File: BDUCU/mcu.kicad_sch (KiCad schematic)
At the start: 15 parts, among them SW1 SW_Push, U8 ATmega328-A, Y1 20MHz

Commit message: BDUCU did stuffs
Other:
- added sheet CAN1 (can_controller.kicad_sch)
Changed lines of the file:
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@@
     )
   )
-  (global_label "CAN0_CS" (shape output) (at 209.55 46.736 180) (fields_autoplaced)
-    (effects (font (size 1.27 1.27)) (justify right))
-    (property "Intersheetrefs" "${INTERSHEET_REFS}" (at 198.2191 46.736 0)
+  (global_label "CAN0_CS" (shape output) (at 209.55 46.355 180) (fields_autoplaced)
+    (effects (font (size 1.27 1.27)) (justify right))
+    (property "Intersheetrefs" "${INTERSHEET_REFS}" (at 198.2191 46.355 0)
       (effects (font (size 1.27 1.27)) (justify right) hide)
     )
@@
     )
   )
+  (global_label "CAN0_H" (shape input) (at 242.57 43.815 0) (fields_autoplaced)
+    (effects (font (size 1.27 1.27)) (justify left))
+    (property "Intersheetrefs" "${INTERSHEET_REFS}" (at 252.7519 43.815 0)
+      (effects (font (size 1.27 1.27)) (justify left) hide)
+    )
+  )
+  (global_label "SCK" (shape output) (at 209.55 66.675 180) (fields_autoplaced)
+    (effects (font (size 1.27 1.27)) (justify right))
+    (property "Intersheetrefs" "${INTERSHEET_REFS}" (at 202.8153 66.675 0)
+      (effects (font (size 1.27 1.27)) (justify right) hide)
+    )
+  )
   (global_label "TS_ACT_5" (shape input) (at 71.374 104.648 0) (fields_autoplaced)
     (effects (font (size 1.27 1.27)) (justify left))
@@
     )
   )
+  (global_label "CAN1_CS" (shape output) (at 209.55 63.5 180) (fields_autoplaced)
+    (effects (font (size 1.27 1.27)) (justify right))
+    (property "Intersheetrefs" "${INTERSHEET_REFS}" (at 198.2191 63.5 0)
+      (effects (font (size 1.27 1.27)) (justify right) hide)
+    )
+  )
   (global_label "RST" (shape input) (at 114.935 117.475 180) (fields_autoplaced)
     (effects (font (size 1.27 1.27)) (justify right))
@@
     )
   )
+  (global_label "MOSI" (shape input) (at 209.55 60.96 180) (fields_autoplaced)
+    (effects (font (size 1.27 1.27)) (justify right))
+    (property "Intersheetrefs" "${INTERSHEET_REFS}" (at 202.048 60.96 0)
+      (effects (font (size 1.27 1.27)) (justify right) hide)
+    )
+  )
   (global_label "AIR+_5" (shape output) (at 71.374 94.488 0) (fields_autoplaced)
     (effects (font (size 1.27 1.27)) (justify left))
@@
     )
   )
+  (global_label "MISO" (shape output) (at 209.55 58.42 180) (fields_autoplaced)
+    (effects (font (size 1.27 1.27)) (justify right))
+    (property "Intersheetrefs" "${INTERSHEET_REFS}" (at 201.9686 58.42 0)
+      (effects (font (size 1.27 1.27)) (justify right) hide)
+    )
+  )
   (global_label "HALL_HI" (shape input) (at 71.374 79.248 0) (fields_autoplaced)
     (effects (font (size 1.27 1.27)) (justify left))
@@
     )
   )
+  (global_label "CAN1_H" (shape input) (at 242.57 60.325 0) (fields_autoplaced)
+    (effects (font (size 1.27 1.27)) (justify left))
+    (property "Intersheetrefs" "${INTERSHEET_REFS}" (at 252.7519 60.325 0)
+      (effects (font (size 1.27 1.27)) (justify left) hide)
+    )
+  )
   (global_label "MOSI" (shape input) (at 71.374 56.388 0) (fields_autoplaced)
     (effects (font (size 1.27 1.27)) (justify left))
@@
     )
   )
-  (global_label "MOSI" (shape input) (at 209.55 44.196 180) (fields_autoplaced)
-    (effects (font (size 1.27 1.27)) (justify right))
-    (property "Intersheetrefs" "${INTERSHEET_REFS}" (at 202.048 44.196 0)
+  (global_label "MOSI" (shape input) (at 209.55 43.815 180) (fields_autoplaced)
+    (effects (font (size 1.27 1.27)) (justify right))
+    (property "Intersheetrefs" "${INTERSHEET_REFS}" (at 202.048 43.815 0)
       (effects (font (size 1.27 1.27)) (justify right) hide)
     )
@@
     )
   )
+  (global_label "CAN0_L" (shape input) (at 242.57 46.355 0) (fields_autoplaced)
+    (effects (font (size 1.27 1.27)) (justify left))
+    (property "Intersheetrefs" "${INTERSHEET_REFS}" (at 252.4495 46.355 0)
+      (effects (font (size 1.27 1.27)) (justify left) hide)
+    )
+  )
   (global_label "CAN0_CS" (shape output) (at 71.374 53.848 0) (fields_autoplaced)
     (effects (font (size 1.27 1.27)) (justify left))
@@
     )
   )
-  (global_label "SCK" (shape output) (at 209.55 49.53 180) (fields_autoplaced)
-    (effects (font (size 1.27 1.27)) (justify right))
-    (property "Intersheetrefs" "${INTERSHEET_REFS}" (at 202.8153 49.53 0)
-      (effects (font (size 1.27 1.27)) (justify right) hide)
-    )
-  )
-  (global_label "MISO" (shape output) (at 209.55 41.656 180) (fields_autoplaced)
-    (effects (font (size 1.27 1.27)) (justify right))
-    (property "Intersheetrefs" "${INTERSHEET_REFS}" (at 201.9686 41.656 0)
+  (global_label "SCK" (shape output) (at 209.55 48.895 180) (fields_autoplaced)
+    (effects (font (size 1.27 1.27)) (justify right))
+    (property "Intersheetrefs" "${INTERSHEET_REFS}" (at 202.8153 48.895 0)
+      (effects (font (size 1.27 1.27)) (justify right) hide)
+    )
+  )
+  (global_label "CAN1_L" (shape input) (at 242.57 62.865 0) (fields_autoplaced)
+    (effects (font (size 1.27 1.27)) (justify left))
+    (property "Intersheetrefs" "${INTERSHEET_REFS}" (at 252.4495 62.865 0)
+      (effects (font (size 1.27 1.27)) (justify left) hide)
+    )
+  )
+  (global_label "MISO" (shape output) (at 209.55 41.275 180) (fields_autoplaced)
+    (effects (font (size 1.27 1.27)) (justify right))
+    (property "Intersheetrefs" "${INTERSHEET_REFS}" (at 201.9686 41.275 0)
       (effects (font (size 1.27 1.27)) (justify right) hide)
     )
@@
     )
   )
-  (sheet (at 209.55 39.624) (size 33.274 11.43) (fields_autoplaced)
+  (sheet (at 209.55 39.37) (size 33.02 11.43) (fields_autoplaced)
     (stroke (width 0.1524) (type solid))
     (fill (color 0 0 0 0.0000))
-    (property "Sheetname" "CAN0" (at 209.55 38.9124 0)
+    (property "Sheetname" "CAN0" (at 209.55 38.6584 0)
       (effects (font (size 1.27 1.27)) (justify left bottom))
     )
-    (property "Sheetfile" "can_controller.kicad_sch" (at 209.55 51.6386 0)
+    (property "Sheetfile" "can_controller.kicad_sch" (at 209.55 51.3846 0)
       (effects (font (size 1.27 1.27)) (justify left top))
     )
-    (pin "MISO" input (at 209.55 41.656 180)
+    (pin "MISO" input (at 209.55 41.275 180)
       (effects (font (size 1.27 1.27)) (justify left))
     )
-    (pin "MOSI" input (at 209.55 44.196 180)
+    (pin "MOSI" input (at 209.55 43.815 180)
       (effects (font (size 1.27 1.27)) (justify left))
     )
-    (pin "CS" input (at 209.55 46.736 180)
+    (pin "CS" input (at 209.55 46.355 180)
       (effects (font (size 1.27 1.27)) (justify left))
     )
-    (pin "SCK" input (at 209.55 49.53 180)
+    (pin "SCK" input (at 209.55 48.895 180)
       (effects (font (size 1.27 1.27)) (justify left))
     )
-    (pin "CAN_H" input (at 242.824 43.688 0)
-      (effects (font (size 1.27 1.27)) (justify right))
-    )
-    (pin "CAN_L" input (at 242.824 46.228 0)
+    (pin "CAN_H" input (at 242.57 43.815 0)
+      (effects (font (size 1.27 1.27)) (justify right))
+    )
+    (pin "CAN_L" input (at 242.57 46.355 0)
       (effects (font (size 1.27 1.27)) (justify right))
     )
@@
       )
     )
+  )
+  (sheet (at 209.55 56.515) (size 33.02 11.43) (fields_autoplaced)
+    (stroke (width 0.1524) (type solid))
+    (fill (color 0 0 0 0.0000))
+    (property "Sheetname" "CAN1" (at 209.55 55.8034 0)
+      (effects (font (size 1.27 1.27)) (justify left bottom))
+    )
+    (property "Sheetfile" "can_controller.kicad_sch" (at 209.55 68.5296 0)
+      (effects (font (size 1.27 1.27)) (justify left top))
+    )
+    (pin "MISO" input (at 209.55 58.42 180)
+      (effects (font (size 1.27 1.27)) (justify left))
+    )
+    (pin "MOSI" input (at 209.55 60.96 180)
+      (effects (font (size 1.27 1.27)) (justify left))
+    )
+    (pin "CS" input (at 209.55 63.5 180)
+      (effects (font (size 1.27 1.27)) (justify left))
+    )
+    (pin "SCK" input (at 209.55 66.675 180)
+      (effects (font (size 1.27 1.27)) (justify left))
+    )
+    (pin "CAN_H" input (at 242.57 60.325 0)
+      (effects (font (size 1.27 1.27)) (justify right))
+    )
+    (pin "CAN_L" input (at 242.57 62.865 0)
+      (effects (font (size 1.27 1.27)) (justify right))
+    )
+    (instances
+      (project "BDUCU"
+        (path "/9942a424-e19d-4ffb-8473-f960b5c811cf/8fc427df-2d97-44b9-b479-5014f2f05880" (page "12"))
+      )
+    )

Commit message: BDUCU COMMIT
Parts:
- AVR-ISP1: footprint Connector_PinHeader_2.54mm:PinHeader_2x03_P2.54mm_Vertical -> Connector_PinHeader_2.54mm:PinHeader_2x03_P2.54mm_Vertical_SMD
- Y1: value 20MHz -> 16MHz
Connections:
- net +5VA is gone; now on net +5V: C20.2, U8.20 (AREF)
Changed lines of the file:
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@@
 	)
 	(junction
-		(at 34.001 48.768)
+		(at 34.29 48.5525)
 		(diameter 0)
 		(color 0 0 0 0)
@@
 	(wire
 		(pts
-			(xy 34.001 48.768) (xy 40.894 48.768)
+			(xy 28.483 48.6795) (xy 33.563 48.6795)
+		)
+		(stroke
+			(width 0)
+			(type default)
+		)
+	)
+	(wire
+		(pts
+			(xy 34.29 48.5525) (xy 38.643 48.5525)
 		)
 		(stroke
@@
 	(wire
 		(pts
-			(xy 34.001 45.9355) (xy 34.001 48.768)
+			(xy 34.29 45.72) (xy 34.29 48.5525)
+		)
+		(stroke
+			(width 0)
+			(type default)
+		)
+	)
+	(wire
+		(pts
+			(xy 28.483 48.895) (xy 29.464 48.895)
 		)
 		(stroke
@@
 	(wire
 		(pts
+			(xy 28.483 48.6795) (xy 28.483 48.895)
+		)
+		(stroke
+			(width 0)
+			(type default)
+		)
+	)
+	(wire
+		(pts
 			(xy 111.76 86.995) (xy 111.76 95.25)
 		)
@@
 	(wire
 		(pts
-			(xy 33.274 48.895) (xy 33.274 48.768)
+			(xy 33.563 48.6795) (xy 33.563 48.5525)
 		)
 		(stroke
@@
 	(wire
 		(pts
+			(xy 38.643 48.768) (xy 40.894 48.768)
+		)
+		(stroke
+			(width 0)
+			(type default)
+		)
+	)
+	(wire
+		(pts
 			(xy 100.965 41.275) (xy 100.965 40.64)
 		)
@@
 	(wire
 		(pts
+			(xy 38.643 48.5525) (xy 38.643 48.768)
+		)
+		(stroke
+			(width 0)
+			(type default)
+		)
+	)
+	(wire
+		(pts
 			(xy 125.73 86.995) (xy 125.73 95.25)
 		)
@@
 	(wire
 		(pts
-			(xy 33.274 48.768) (xy 34.001 48.768)
-		)
-		(stroke
-			(width 0)
-			(type default)
-		)
-	)
-	(wire
-		(pts
-			(xy 29.464 48.895) (xy 33.274 48.895)
+			(xy 33.563 48.5525) (xy 34.29 48.5525)
 		)
 		(stroke
@@
 				(path "/9942a424-e19d-4ffb-8473-f960b5c811cf/8fc427df-2d97-44b9-b479-5014f2f05880"
 					(reference "D3")
+					(unit 1)
+				)
+			)
+		)
+	)
+	(symbol
+		(lib_id "power:+5V")
+		(at 34.29 45.72 0)
+		(unit 1)
+		(exclude_from_sim no)
+		(in_bom yes)
+		(on_board yes)
+		(dnp no)
+		(fields_autoplaced yes)
+		(property "Reference" "#PWR033"
+			(at 34.29 49.53 0)
+			(effects
+				(font
+					(size 1.27 1.27)
+				)
+				(hide yes)
+			)
+		)
+		(property "Value" "+5V"
+			(at 34.29 40.64 0)
+			(effects
+				(font
+					(size 1.27 1.27)
+				)
+			)
+		)
+		(property "Footprint" ""
+			(at 34.29 45.72 0)
+			(effects
+				(font
+					(size 1.27 1.27)
+				)
+				(hide yes)
+			)
+		)
+		(property "Datasheet" ""
+			(at 34.29 45.72 0)
+			(effects
+				(font
+					(size 1.27 1.27)
+				)
+				(hide yes)
+			)
+		)
+		(property "Description" ""
+			(at 34.29 45.72 0)
+			(effects
+				(font
+					(size 1.27 1.27)
+				)
+			)
+		)
+		(pin "1"
+		)
+		(instances
+			(project "BDUCU"
+				(path "/9942a424-e19d-4ffb-8473-f960b5c811cf/8fc427df-2d97-44b9-b479-5014f2f05880"
+					(reference "#PWR033")
 					(unit 1)
 				)
@@
 			)
 		)
-		(property "Footprint" "Connector_PinHeader_2.54mm:PinHeader_2x03_P2.54mm_Vertical"
+		(property "Footprint" "Connector_PinHeader_2.54mm:PinHeader_2x03_P2.54mm_Vertical_SMD"
 			(at 120.015 114.935 0)
 			(effects
@@
 	)
 	(symbol
-		(lib_id "power:+5VA")
-		(at 34.001 45.9355 0)
-		(unit 1)
-		(exclude_from_sim no)
-		(in_bom yes)
-		(on_board yes)
-		(dnp no)
-		(fields_autoplaced yes)
-		(property "Reference" "#PWR035"
-			(at 34.001 49.7455 0)
-			(effects
-				(font
-					(size 1.27 1.27)
-				)
-				(hide yes)
-			)
-		)
-		(property "Value" "+5VA"
-			(at 34.001 40.8555 0)
-			(effects
-				(font
-					(size 1.27 1.27)
-				)
-			)
-		)
-		(property "Footprint" ""
-			(at 34.001 45.9355 0)
-			(effects
-				(font
-					(size 1.27 1.27)
-				)
-				(hide yes)
-			)
-		)
-		(property "Datasheet" ""
-			(at 34.001 45.9355 0)
-			(effects
-				(font
-					(size 1.27 1.27)
-				)
-				(hide yes)
-			)
-		)
-		(property "Description" ""
-			(at 34.001 45.9355 0)
-			(effects
-				(font
-					(size 1.27 1.27)
-				)
-			)
-		)
-		(pin "1"
-		)
-		(instances
-			(project "BDUCU"
-				(path "/9942a424-e19d-4ffb-8473-f960b5c811cf/8fc427df-2d97-44b9-b479-5014f2f05880"
-					(reference "#PWR035")
-					(unit 1)
-				)
-			)
-		)
-	)
-	(symbol
 		(lib_id "Device:C")
 		(at 100.965 36.83 180)
@@
 			)
 		)
-		(property "Value" "20MHz"
+		(property "Value" "16MHz"
 			(at 104.775 64.008 90)
 			(effects
@@
 		(exclude_from_sim no)
 		(in_bom yes)
-		(on_board no)
+		(on_board yes)
 		(dnp no)
 		(property "Reference" "C20"

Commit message: BDUCU finalised
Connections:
- net CAN0_CS: now also U8.13 (PB1); no longer U8.14 (PB2)
- net CAN1_CS: now also U8.14 (PB2); no longer U8.13 (PB1)
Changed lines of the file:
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@@
 	(global_label "CAN0_CS"
 		(shape output)
-		(at 71.374 53.848 0)
+		(at 71.374 51.308 0)
 		(fields_autoplaced yes)
 		(effects
@@
 		)
 		(property "Intersheetrefs" "${INTERSHEET_REFS}"
-			(at 82.7049 53.848 0)
+			(at 82.7049 51.308 0)
 			(effects
 				(font
@@
 	(global_label "CAN1_CS"
 		(shape output)
-		(at 71.374 51.308 0)
+		(at 71.374 53.848 0)
 		(fields_autoplaced yes)
 		(effects
@@
 		)
 		(property "Intersheetrefs" "${INTERSHEET_REFS}"
-			(at 82.7049 51.308 0)
+			(at 82.7049 53.848 0)
 			(effects
 				(font

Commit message: Finished BDUCU layout, silkscreen remaining
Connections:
- net AIR+_5: now also U8.32 (PD2); no longer U8.31 (PD1)
- net AIR-_5: now also U8.31 (PD1); no longer U8.30 (PD0)
- net AMS_ERR: now also U8.30 (PD0); no longer U8.1 (PD3)
- net PRE_5: now also U8.9 (PD5); no longer U8.32 (PD2)
- net SDC_5: now also U8.11 (PD7); no longer U8.2 (PD4)
- net TS_ACT_5: now also U8.10 (PD6); no longer U8.9 (PD5)
- net INPUT2_5V: now reaches U8.12 (PB0)
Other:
- moved on the sheet: AVR-ISP1, C16, C17, C18, C20, C21, C22, R17, R22, SW1, U8, Y1

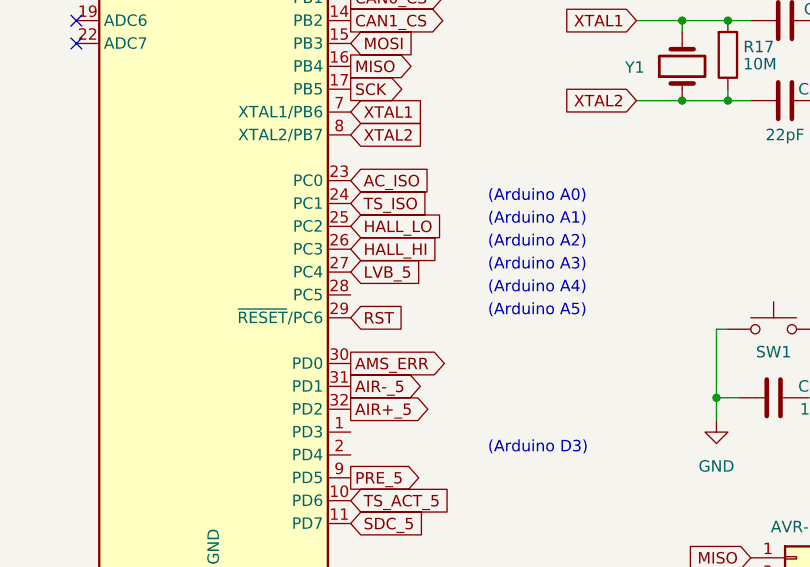
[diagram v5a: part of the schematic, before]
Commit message: bducu done I think added ntc
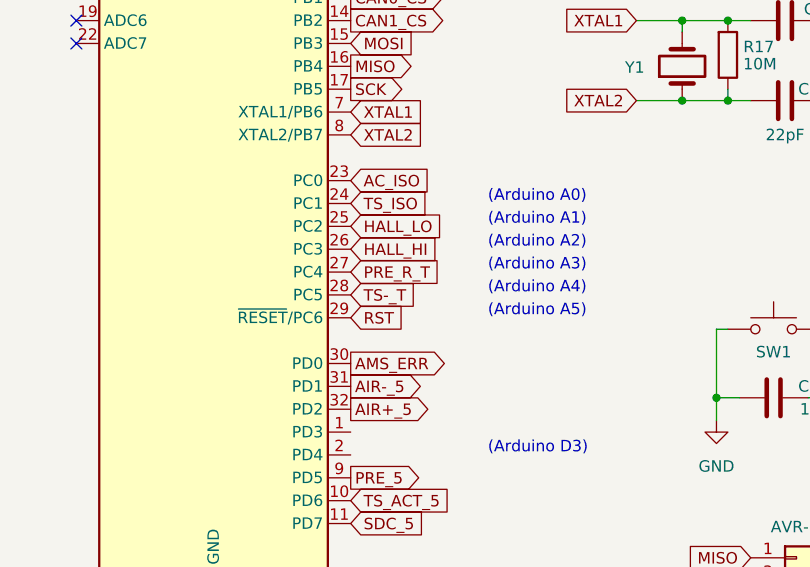
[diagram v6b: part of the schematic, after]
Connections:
- net TS-_T: now reaches U8.28 (PC5)
- net LVB_5 renamed PRE_R_T
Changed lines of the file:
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@@
 		)
 	)
-	(global_label "LVB_5"
+	(global_label "XTAL2"
+		(shape input)
+		(at 71.12 66.04 0)
+		(fields_autoplaced yes)
+		(effects
+			(font
+				(size 1.27 1.27)
+			)
+			(justify left)
+		)
+		(property "Intersheetrefs" "${INTERSHEET_REFS}"
+			(at 79.6085 66.04 0)
+			(effects
+				(font
+					(size 1.27 1.27)
+				)
+				(justify left)
+				(hide yes)
+			)
+		)
+	)
+	(global_label "CAN1_H"
+		(shape input)
+		(at 242.57 62.23 0)
+		(fields_autoplaced yes)
+		(effects
+			(font
+				(size 1.27 1.27)
+			)
+			(justify left)
+		)
+		(property "Intersheetrefs" "${INTERSHEET_REFS}"
+			(at 252.7519 62.23 0)
+			(effects
+				(font
+					(size 1.27 1.27)
+				)
+				(justify left)
+				(hide yes)
+			)
+		)
+	)
+	(global_label "SDC_5"
+		(shape input)
+		(at 71.12 109.22 0)
+		(fields_autoplaced yes)
+		(effects
+			(font
+				(size 1.27 1.27)
+			)
+			(justify left)
+		)
+		(property "Intersheetrefs" "${INTERSHEET_REFS}"
+			(at 80.8181 109.22 0)
+			(effects
+				(font
+					(size 1.27 1.27)
+				)
+				(justify left)
+				(hide yes)
+			)
+		)
+	)
+	(global_label "MOSI"
+		(shape input)
+		(at 71.12 55.88 0)
+		(fields_autoplaced yes)
+		(effects
+			(font
+				(size 1.27 1.27)
+			)
+			(justify left)
+		)
+		(property "Intersheetrefs" "${INTERSHEET_REFS}"
+			(at 78.622 55.88 0)
+			(effects
+				(font
+					(size 1.27 1.27)
+				)
+				(justify left)
+				(hide yes)
+			)
+		)
+	)
+	(global_label "PRE_R_T"
 		(shape input)
 		(at 71.12 81.28 0)
@@
 		)
 		(property "Intersheetrefs" "${INTERSHEET_REFS}"
-			(at 79.669 81.28 0)
-			(effects
-				(font
-					(size 1.27 1.27)
-				)
-				(justify left)
+			(at 81.967 81.28 0)
+			(effects
+				(font
+					(size 1.27 1.27)
+				)
+				(justify left)
+				(hide yes)
+			)
+		)
+	)
+	(global_label "MOSI"
+		(shape input)
+		(at 128.27 115.57 0)
+		(fields_autoplaced yes)
+		(effects
+			(font
+				(size 1.27 1.27)
+			)
+			(justify left)
+		)
+		(property "Intersheetrefs" "${INTERSHEET_REFS}"
+			(at 135.772 115.57 0)
+			(effects
+				(font
+					(size 1.27 1.27)
+				)
+				(justify left)
+				(hide yes)
+			)
+		)
+	)
+	(global_label "XTAL1"
+		(shape input)
+		(at 71.12 63.5 0)
+		(fields_autoplaced yes)
+		(effects
+			(font
+				(size 1.27 1.27)
+			)
+			(justify left)
+		)
+		(property "Intersheetrefs" "${INTERSHEET_REFS}"
+			(at 79.6085 63.5 0)
+			(effects
+				(font
+					(size 1.27 1.27)
+				)
+				(justify left)
+				(hide yes)
+			)
+		)
+	)
+	(global_label "SCK"
+		(shape input)
+		(at 115.57 115.57 180)
+		(fields_autoplaced yes)
+		(effects
+			(font
+				(size 1.27 1.27)
+			)
+			(justify right)
+		)
+		(property "Intersheetrefs" "${INTERSHEET_REFS}"
+			(at 108.9147 115.57 0)
+			(effects
+				(font
+					(size 1.27 1.27)
+				)
+				(justify right)
+				(hide yes)
+			)
+		)
+	)
+	(global_label "MOSI"
+		(shape input)
+		(at 209.55 44.45 180)
+		(fields_autoplaced yes)
+		(effects
+			(font
+				(size 1.27 1.27)
+			)
+			(justify right)
+		)
+		(property "Intersheetrefs" "${INTERSHEET_REFS}"
+			(at 202.048 44.45 0)
+			(effects
+				(font
+					(size 1.27 1.27)
+				)
+				(justify right)
 				(hide yes)
 			)
@@
 	(global_label "XTAL2"
 		(shape input)
-		(at 71.12 66.04 0)
-		(fields_autoplaced yes)
-		(effects
-			(font
-				(size 1.27 1.27)
-			)
-			(justify left)
-		)
-		(property "Intersheetrefs" "${INTERSHEET_REFS}"
-			(at 79.6085 66.04 0)
-			(effects
-				(font
-					(size 1.27 1.27)
-				)
-				(justify left)
-				(hide yes)
-			)
-		)
-	)
-	(global_label "CAN1_H"
-		(shape input)
-		(at 242.57 62.23 0)
-		(fields_autoplaced yes)
-		(effects
-			(font
-				(size 1.27 1.27)
-			)
-			(justify left)
-		)
-		(property "Intersheetrefs" "${INTERSHEET_REFS}"
-			(at 252.7519 62.23 0)
-			(effects
-				(font
-					(size 1.27 1.27)
-				)
-				(justify left)
-				(hide yes)
-			)
-		)
-	)
-	(global_label "SDC_5"
-		(shape input)
-		(at 71.12 109.22 0)
-		(fields_autoplaced yes)
-		(effects
-			(font
-				(size 1.27 1.27)
-			)
-			(justify left)
-		)
-		(property "Intersheetrefs" "${INTERSHEET_REFS}"
-			(at 80.8181 109.22 0)
-			(effects
-				(font
-					(size 1.27 1.27)
-				)
-				(justify left)
-				(hide yes)
-			)
-		)
-	)
-	(global_label "MOSI"
-		(shape input)
-		(at 71.12 55.88 0)
-		(fields_autoplaced yes)
-		(effects
-			(font
-				(size 1.27 1.27)
-			)
-			(justify left)
-		)
-		(property "Intersheetrefs" "${INTERSHEET_REFS}"
-			(at 78.622 55.88 0)
-			(effects
-				(font
-					(size 1.27 1.27)
-				)
-				(justify left)
-				(hide yes)
-			)
-		)
-	)
-	(global_label "MOSI"
-		(shape input)
-		(at 128.27 115.57 0)
-		(fields_autoplaced yes)
-		(effects
-			(font
-				(size 1.27 1.27)
-			)
-			(justify left)
-		)
-		(property "Intersheetrefs" "${INTERSHEET_REFS}"
-			(at 135.772 115.57 0)
-			(effects
-				(font
-					(size 1.27 1.27)
-				)
-				(justify left)
-				(hide yes)
-			)
-		)
-	)
-	(global_label "XTAL1"
-		(shape input)
-		(at 71.12 63.5 0)
-		(fields_autoplaced yes)
-		(effects
-			(font
-				(size 1.27 1.27)
-			)
-			(justify left)
-		)
-		(property "Intersheetrefs" "${INTERSHEET_REFS}"
-			(at 79.6085 63.5 0)
-			(effects
-				(font
-					(size 1.27 1.27)
-				)
-				(justify left)
-				(hide yes)
-			)
-		)
-	)
-	(global_label "SCK"
-		(shape input)
-		(at 115.57 115.57 180)
+		(at 102.87 62.23 180)
 		(fields_autoplaced yes)
 		(effects
@@
 		)
 		(property "Intersheetrefs" "${INTERSHEET_REFS}"
-			(at 108.9147 115.57 0)
+			(at 94.3815 62.23 0)
 			(effects
 				(font
@@
 		)
 	)
-	(global_label "MOSI"
-		(shape input)
-		(at 209.55 44.45 180)
-		(fields_autoplaced yes)
-		(effects
-			(font
-				(size 1.27 1.27)
-			)
-			(justify right)
-		)
-		(property "Intersheetrefs" "${INTERSHEET_REFS}"
-			(at 202.048 44.45 0)
-			(effects
-				(font
-					(size 1.27 1.27)
-				)
-				(justify right)
-				(hide yes)
-			)
-		)
-	)
-	(global_label "XTAL2"
-		(shape input)
-		(at 102.87 62.23 180)
-		(fields_autoplaced yes)
-		(effects
-			(font
-				(size 1.27 1.27)
-			)
-			(justify right)
-		)
-		(property "Intersheetrefs" "${INTERSHEET_REFS}"
-			(at 94.3815 62.23 0)
-			(effects
-				(font
-					(size 1.27 1.27)
-				)
-				(justify right)
-				(hide yes)
-			)
+	(global_label "TS-_T"
+		(shape input)
+		(at 71.12 83.82 0)
+		(fields_autoplaced yes)
+		(effects
+			(font
+				(size 1.27 1.27)
+			)
+			(justify left)
+		)
+		(property "Intersheetrefs" "${INTERSHEET_REFS}"
+			(at 79.7899 83.82 0)
+			(effects
+				(font
+					(size 1.27 1.27)
+				)
+				(justify left)
+				(hide yes)
+			)

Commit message: I am Nicholas Chan (lesbian version)
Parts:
- renumbered C20 to C22, C16 to C23, C17 to C24, C23 to C25, C21 to C26, C22 to C27, C18 to C28, R17 to R28, R25 to R29, R22 to R30, U8 to U12, Y1 to Y2
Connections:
- net AIR+_5: now also U12.2 (PD4); no longer U12.32 (PD2)
- net INT_1: now reaches U12.1 (PD3)
- new net INT_0: U12.32 (PD2)
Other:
- sheet CAN0 ports: added INT; removed none
- sheet CAN1 ports: added INT; removed none
